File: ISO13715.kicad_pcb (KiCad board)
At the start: 2 copper layers, 123.8 x 67.9 mm, 39 parts, among them U1 Seeeduino Xiao rp2040

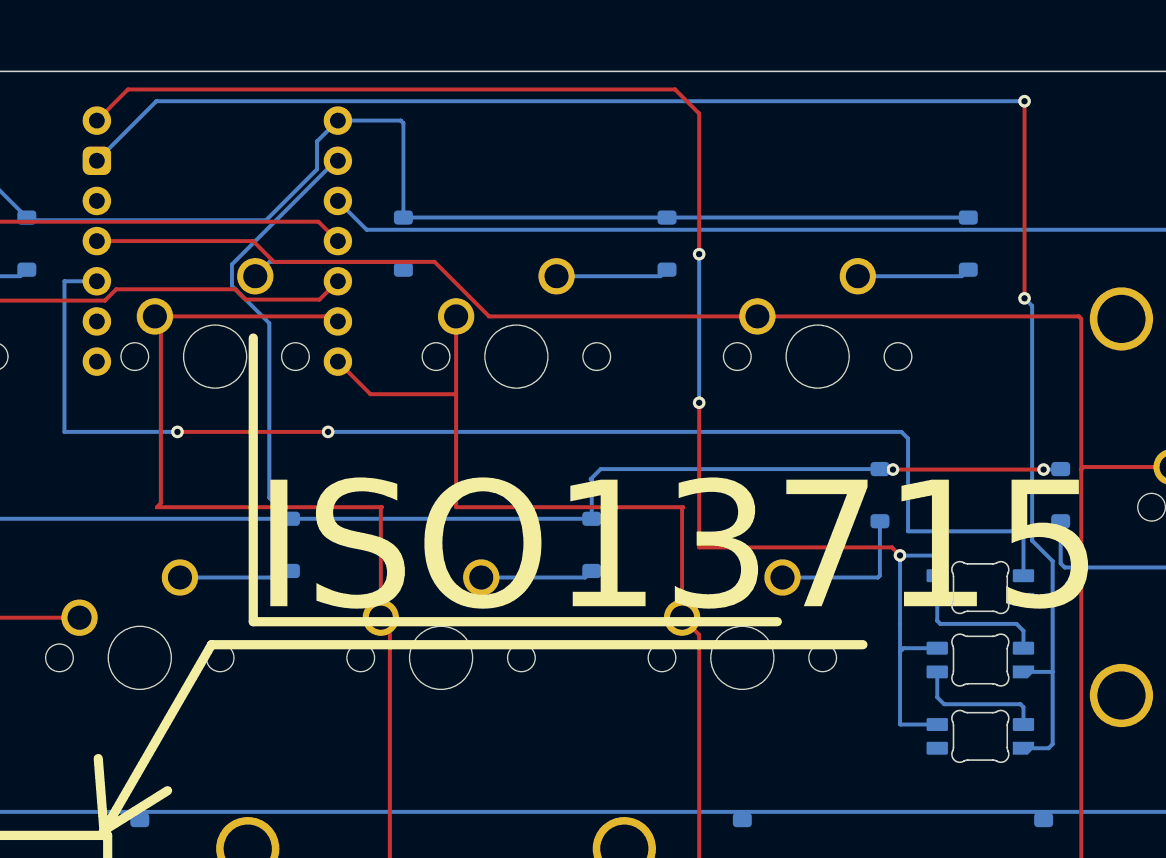
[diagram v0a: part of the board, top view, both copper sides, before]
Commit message: changed GND to plane
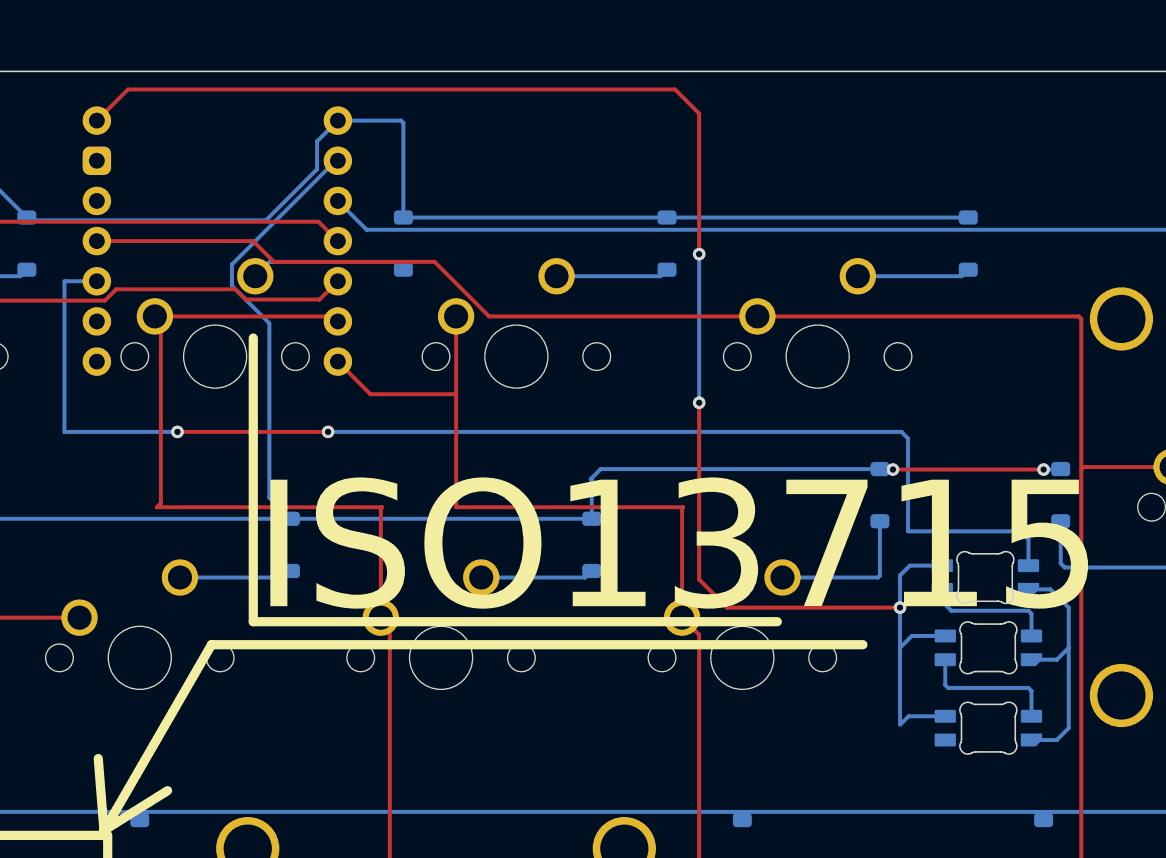
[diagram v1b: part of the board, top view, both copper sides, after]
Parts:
- moved LED2 0.93 mm to (148.9, 89.9)
- moved LED3 0.73 mm to (148.9, 94.9)
- moved LED1 0.71 mm to (148.7, 85.4)
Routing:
- net GND: track 107.4 -> 16.0 mm, vias 2 -> 0
- net VCC_5V: track 99.3 -> 101.0 mm
- net D_in: track 81.2 -> 80.4 mm
- added copper zone on B.Cu, net GND
- removed copper zone on B.Cu, net (none)

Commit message: updated PCB and readme
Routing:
- net Row1: track 96.8 -> 99.8 mm
- net Col2: track 64.2 -> 63.6 mm
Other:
- board text added: "ISO13715 by exen904 V1.1"
- board text added: "Xiao face up WS Zero/0xCB Gemini face down"
- board text removed: "ISO13715 by exen904"
- board text removed: "MCU right way up"
